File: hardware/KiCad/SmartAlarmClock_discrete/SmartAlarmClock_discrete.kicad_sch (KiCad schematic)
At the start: 24 parts, among them J1 YD-ESP32-S3 dev board, J2 MAX7219 32x8 module, J3 Touch electrode, Q1 BSS138, Q2 BSS138, Q3 BSS138, Q4 BS170, U1 DS3231MZ

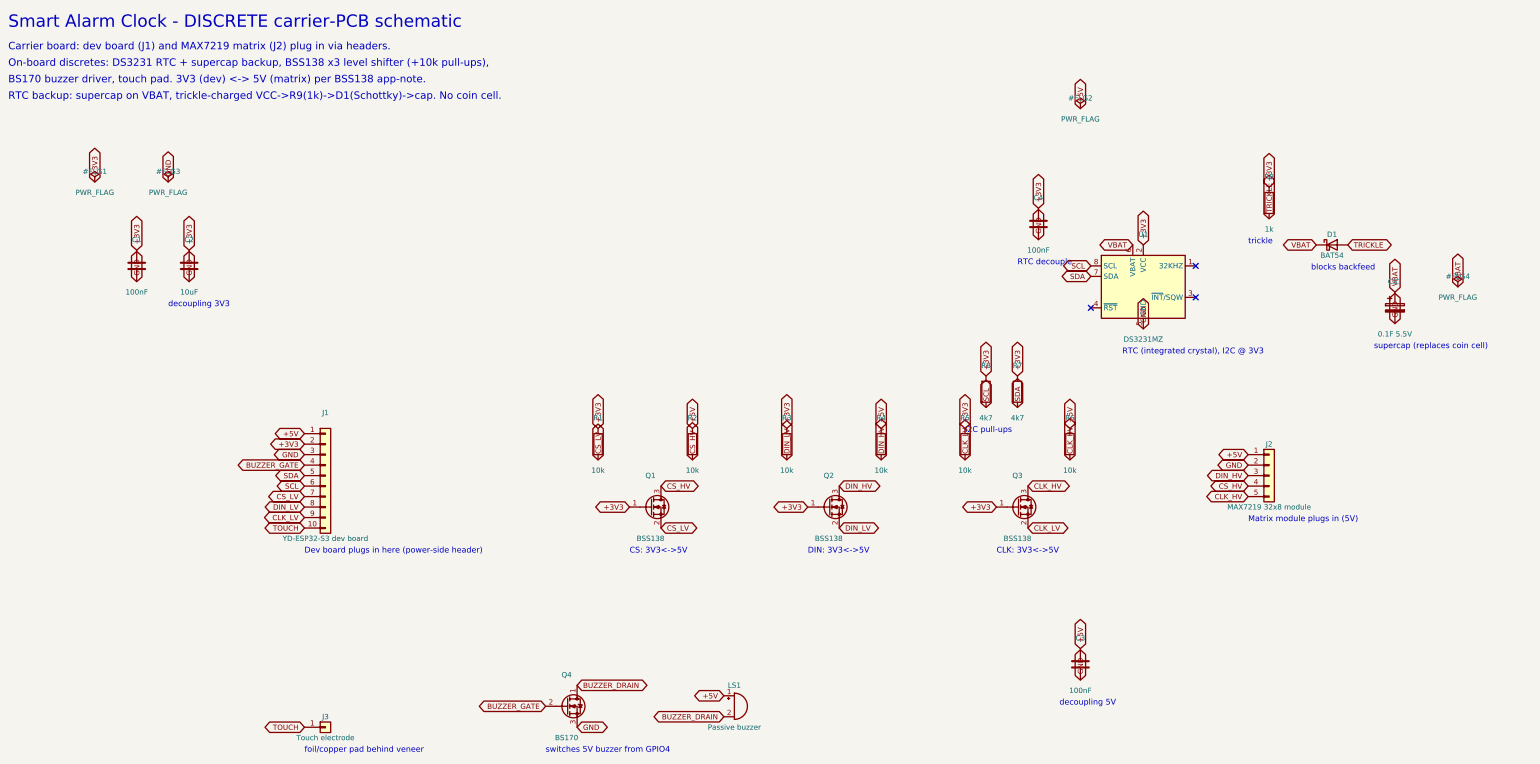
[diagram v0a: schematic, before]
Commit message: hardware: tidy discrete schematic layout
Move ref/value of vertical passives (R/C) to the side so they no longer overlap
the vertical global-label net names. Align the three level-shifter channels,
group the RTC + supercap section, and pull the whole sheet closer together.
Re-render the PNG. ERC still 0/0.

Co-Authored-By: Claude Opus 4.8 (1M context) <noreply@anthropic.com>
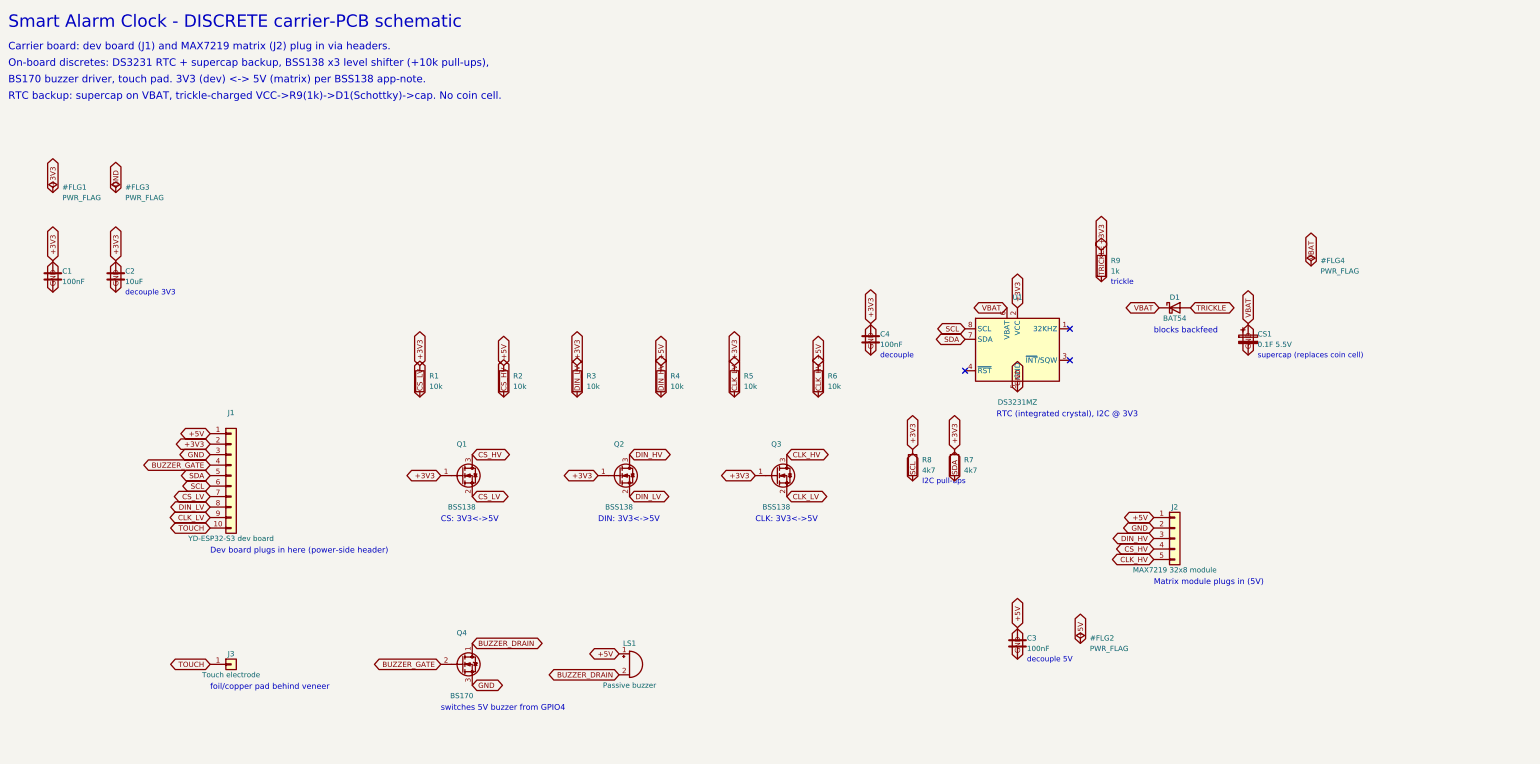
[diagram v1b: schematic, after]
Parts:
- removed R9: 1k, symbol Device:R
- added Q4: BS170, symbol Transistor_FET:BS170
- R9: renamed from Q4; value BS170 -> 1k; symbol Transistor_FET:BS170 -> Device:R
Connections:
- net +3V3: now also R9.1
- net BUZZER_DRAIN: now also Q4.1 (D); no longer R9.1 (D)
- net BUZZER_GATE: now also Q4.2 (G); no longer R9.2 (G)
- net GND: now also Q4.3 (S); no longer R9.3 (S)
- net TRICKLE: now also R9.2
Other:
- note added: "decouple"
- note added: "decouple 3V3"
- note added: "decouple 5V"
- note removed: "RTC decouple"
- note removed: "decoupling 3V3"
- note removed: "decoupling 5V"
- moved on the sheet: J1
